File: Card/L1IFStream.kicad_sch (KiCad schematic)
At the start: 107 parts, among them J1 Conn_Coaxial, J2 USB_A, J3 RF_Shield_One_Piece, J4 Conn_Coaxial, U1 MAX2769ETI+T, U10 74LVC374, U11 74HC2GU04, U2 TPS717285DCKR, U3 TPS717285DCKR, U4 NCP164CSN330T1G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

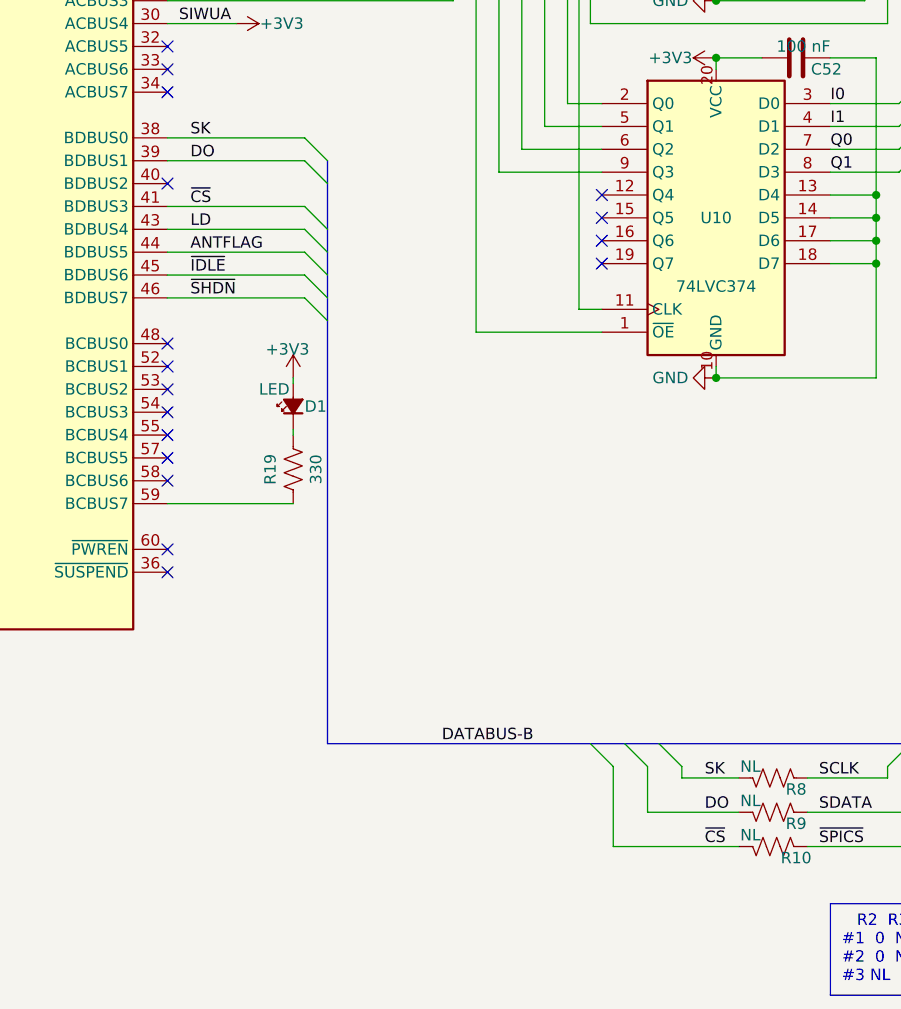
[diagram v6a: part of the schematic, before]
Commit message: Added test points to attach SPI device
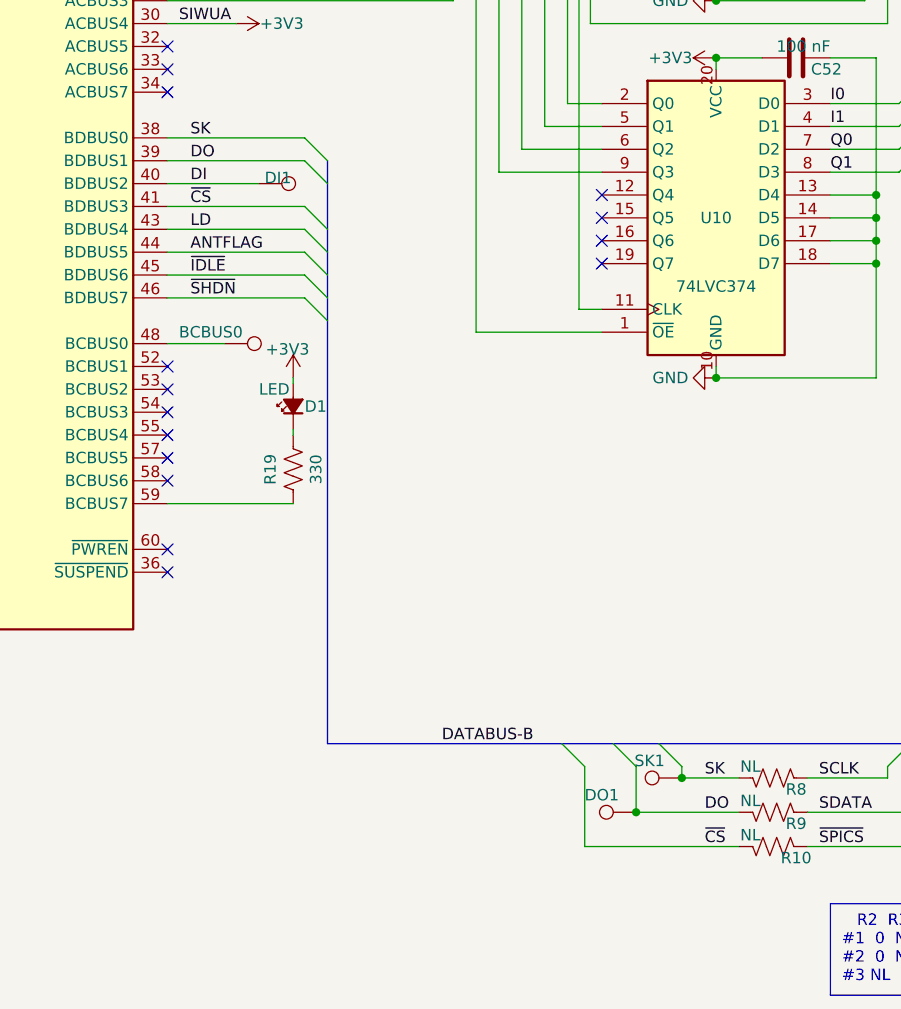
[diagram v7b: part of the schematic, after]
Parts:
- added BCBUS0, DI1, DO1, SK1: TestPoint, L1IFStream:TestPoint_Pad_D1.0mm, symbol Connector:TestPoint
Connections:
- net DO: now also DO1.1
- net SK: now also SK1.1
- net DI: now reaches U6.40 (BDBUS2)
- net DI: now also DI1.1
- net at U6.48 (BCBUS0): now also BCBUS0.1
- no-connect marks 26 -> 24
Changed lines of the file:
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@@
   (junction (at 285.75 38.1) (diameter 0) (color 0 0 0 0)
   )
+  (junction (at 196.85 182.88) (diameter 0) (color 0 0 0 0)
+  )
   (junction (at 156.21 46.99) (diameter 0) (color 0 0 0 0)
   )
@@
   (junction (at 119.38 166.37) (diameter 0) (color 0 0 0 0)
   )
+  (junction (at 201.93 179.07) (diameter 0) (color 0 0 0 0)
+  )
   (junction (at 261.62 172.72) (diameter 0) (color 0 0 0 0)
   )
@@
   )
   (no_connect (at 144.78 85.09))
-  (no_connect (at 144.78 130.81))
   (no_connect (at 193.04 119.38))
   (no_connect (at 257.81 93.98))
@@
   (no_connect (at 144.78 153.67))
   (no_connect (at 144.78 146.05))
-  (no_connect (at 144.78 113.03))
   (no_connect (at 193.04 72.39))
   (no_connect (at 144.78 100.33))
@@
     (stroke (width 0) (type default))
   )
-  (bus_entry (at 191.77 175.26) (size 2.54 2.54)
+  (bus_entry (at 188.595 175.26) (size 2.54 2.54)
     (stroke (width 0) (type default))
   )
@@
     (stroke (width 0) (type default))
   )
-  (bus_entry (at 195.58 175.26) (size 2.54 2.54)
+  (bus_entry (at 194.31 175.26) (size 2.54 2.54)
     (stroke (width 0) (type default))
   )
@@
     (stroke (width 0) (type default))
   )
-  (wire (pts (xy 198.12 182.88) (xy 198.12 177.8))
+  (wire (pts (xy 196.85 182.88) (xy 196.85 177.8))
     (stroke (width 0) (type default))
   )
@@
     (stroke (width 0) (type default))
   )
-  (bus (pts (xy 191.77 175.26) (xy 162.56 175.26))
-    (stroke (width 0) (type default))
-  )
   (wire (pts (xy 44.45 95.25) (xy 45.72 95.25))
     (stroke (width 0) (type default))
@@
     (stroke (width 0) (type default))
   )
+  (bus (pts (xy 188.595 175.26) (xy 162.56 175.26))
+    (stroke (width 0) (type default))
+  )
   (wire (pts (xy 287.02 148.59) (xy 287.02 149.86))
     (stroke (width 0) (type default))
@@
     (stroke (width 0) (type default))
   )
-  (wire (pts (xy 208.28 182.88) (xy 198.12 182.88))
-    (stroke (width 0) (type default))
-  )
   (wire (pts (xy 181.61 111.76) (xy 181.61 80.01))
     (stroke (width 0) (type default))
@@
     (stroke (width 0) (type default))
   )
+  (wire (pts (xy 144.78 113.03) (xy 154.94 113.03))
+    (stroke (width 0) (type default))
+  )
   (wire (pts (xy 111.76 166.37) (xy 114.3 166.37))
     (stroke (width 0) (type default))
@@
     (stroke (width 0) (type default))
   )
+  (wire (pts (xy 191.135 186.69) (xy 208.28 186.69))
+    (stroke (width 0) (type default))
+  )
   (bus (pts (xy 251.46 165.1) (xy 251.46 167.64))
     (stroke (width 0) (type default))
@@
     (stroke (width 0) (type default))
   )
-  (wire (pts (xy 194.31 186.69) (xy 194.31 177.8))
+  (wire (pts (xy 191.135 186.69) (xy 191.135 177.8))
     (stroke (width 0) (type default))
   )
@@
     (stroke (width 0) (type default))
   )
-  (wire (pts (xy 208.28 186.69) (xy 194.31 186.69))
-    (stroke (width 0) (type default))
-  )
   (bus (pts (xy 251.46 172.72) (xy 251.46 175.26))
     (stroke (width 0) (type default))
@@
     (stroke (width 0) (type default))
   )
+  (wire (pts (xy 196.85 182.88) (xy 208.28 182.88))
+    (stroke (width 0) (type default))
+  )
   (wire (pts (xy 123.19 34.29) (xy 123.19 33.02))
     (stroke (width 0) (type default))
@@
     (stroke (width 0) (type default))
   )
-  (bus (pts (xy 191.77 175.26) (xy 195.58 175.26))
+  (bus (pts (xy 188.595 175.26) (xy 194.31 175.26))
     (stroke (width 0) (type default))
   )
@@
     (stroke (width 0) (type default))
   )
+  (wire (pts (xy 144.78 130.81) (xy 151.13 130.81))
+    (stroke (width 0) (type default))
+  )
   (wire (pts (xy 191.77 19.05) (xy 196.85 19.05))
     (stroke (width 0) (type default))
@@
     (stroke (width 0) (type default))
   )
-  (bus (pts (xy 195.58 175.26) (xy 199.39 175.26))
+  (bus (pts (xy 194.31 175.26) (xy 199.39 175.26))
     (stroke (width 0) (type default))
   )
@@
     (effects (font (size 1.27 1.27)) (justify left bottom))
   )
+  (label "DI" (at 147.32 113.03 0) (fields_autoplaced)
+    (effects (font (size 1.27 1.27)) (justify left bottom))
+  )
   (label "LNA2" (at 245.11 78.74 180) (fields_autoplaced)
     (effects (font (size 1.27 1.27)) (justify right bottom))
@@
     )
   )
+  (symbol (lib_id "Connector:TestPoint") (at 196.85 182.88 90) (unit 1)
+    (in_bom yes) (on_board yes) (dnp no)
+    (property "Reference" "DO1" (at 194.945 180.975 90)
+      (effects (font (size 1.27 1.27)) (justify left))
+    )
+    (property "Value" "TestPoint" (at 196.1642 181.4068 0)
+      (effects (font (size 1.27 1.27)) (justify left) hide)
+    )
+    (property "Footprint" "L1IFStream:TestPoint_Pad_D1.0mm" (at 196.85 177.8 0)
+      (effects (font (size 1.27 1.27)) hide)
+    )
+    (property "Datasheet" "~" (at 196.85 177.8 0)
+      (effects (font (size 1.27 1.27)) hide)
+    )
+    (pin "1")
+    (instances
+      (project "L1IFStream"
+        (path "/e22d8814-0b83-456b-8939-db783783fcf1"
+          (reference "DO1") (unit 1)
+        )
+      )
+    )
+  )
   (symbol (lib_id "L1IFStream-rescue:74LVC374-MAX2769FT2232H") (at 205.74 116.84 0) (unit 1)
     (in_bom yes) (on_board yes) (dnp no)
@@
     )
   )
+  (symbol (lib_id "Connector:TestPoint") (at 151.13 130.81 270) (unit 1)
+    (in_bom yes) (on_board yes) (dnp no)
+    (property "Reference" "BCBUS0" (at 146.05 129.54 90)
+      (effects (font (size 1.27 1.27)) (justify left))
+    )
+    (property "Value" "TestPoint" (at 151.8158 132.2832 0)
+      (effects (font (size 1.27 1.27)) (justify left) hide)
+    )
+    (property "Footprint" "L1IFStream:TestPoint_Pad_D1.0mm" (at 151.13 135.89 0)
+      (effects (font (size 1.27 1.27)) hide)
+    )
+    (property "Datasheet" "~" (at 151.13 135.89 0)
+      (effects (font (size 1.27 1.27)) hide)
+    )
+    (pin "1")
+    (instances
+      (project "L1IFStream"
+        (path "/e22d8814-0b83-456b-8939-db783783fcf1"
+          (reference "BCBUS0") (unit 1)
+        )
+      )
+    )
+  )
   (symbol (lib_id "L1IFStream-rescue:R_US-MAX2769FT2232H") (at 331.47 87.63 0) (unit 1)
     (in_bom yes) (on_board yes) (dnp no)
@@
     )
   )
+  (symbol (lib_id "Connector:TestPoint") (at 201.93 179.07 90) (unit 1)
+    (in_bom yes) (on_board yes) (dnp no)
+    (property "Reference" "SK1" (at 200.025 177.165 90)
+      (effects (font (size 1.27 1.27)) (justify left))
+    )
+    (property "Value" "TestPoint" (at 201.2442 177.5968 0)
+      (effects (font (size 1.27 1.27)) (justify left) hide)
+    )
+    (property "Footprint" "L1IFStream:TestPoint_Pad_D1.0mm" (at 201.93 173.99 0)
+      (effects (font (size 1.27 1.27)) hide)
+    )
+    (property "Datasheet" "~" (at 201.93 173.99 0)
+      (effects (font (size 1.27 1.27)) hide)
+    )
+    (pin "1")
+    (instances
+      (project "L1IFStream"
+        (path "/e22d8814-0b83-456b-8939-db783783fcf1"
+          (reference "SK1") (unit 1)
+        )
+      )
+    )
+  )
   (symbol (lib_id "L1IFStream-rescue:C-MAX2769FT2232H") (at 335.915 83.82 90) (mirror x) (unit 1)
     (in_bom yes) (on_board yes) (dnp no)
@@
         )
       )
+    )
+  )
+  (symbol (lib_id "Connector:TestPoint") (at 154.94 113.03 270) (unit 1)
+    (in_bom yes) (on_board yes) (dnp no)
+    (property "Reference" "DI1" (at 155.575 112.395 90)
+      (effects (font (size 1.27 1.27)) (justify left))
+    )
+    (property "Value" "TestPoint" (at 155.6258 114.5032 0)
+      (effects (font (size 1.27 1.27)) (justify left) hide)
+    )
+    (property "Footprint" "L1IFStream:TestPoint_Pad_D1.0mm" (at 154.94 118.11 0)
+      (effects (font (size 1.27 1.27)) hide)
+    )
+    (property "Datasheet" "~" (at 154.94 118.11 0)
+      (effects (font (size 1.27 1.27)) hide)
+    )
+    (pin "1")
+    (instances
+      (project "L1IFStream"
+        (path "/e22d8814-0b83-456b-8939-db783783fcf1"
+          (reference "DI1") (unit 1)
+        )
+      )

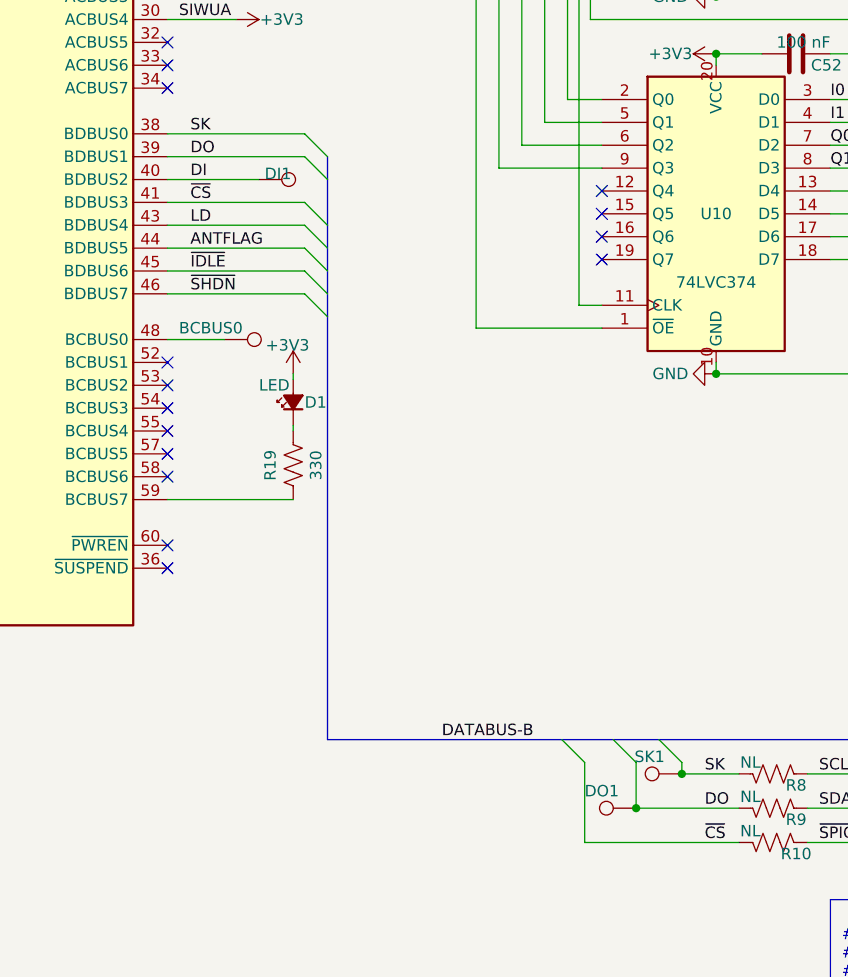
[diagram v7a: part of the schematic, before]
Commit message: Debating how much to fix. Current Argument, just the LED circuit
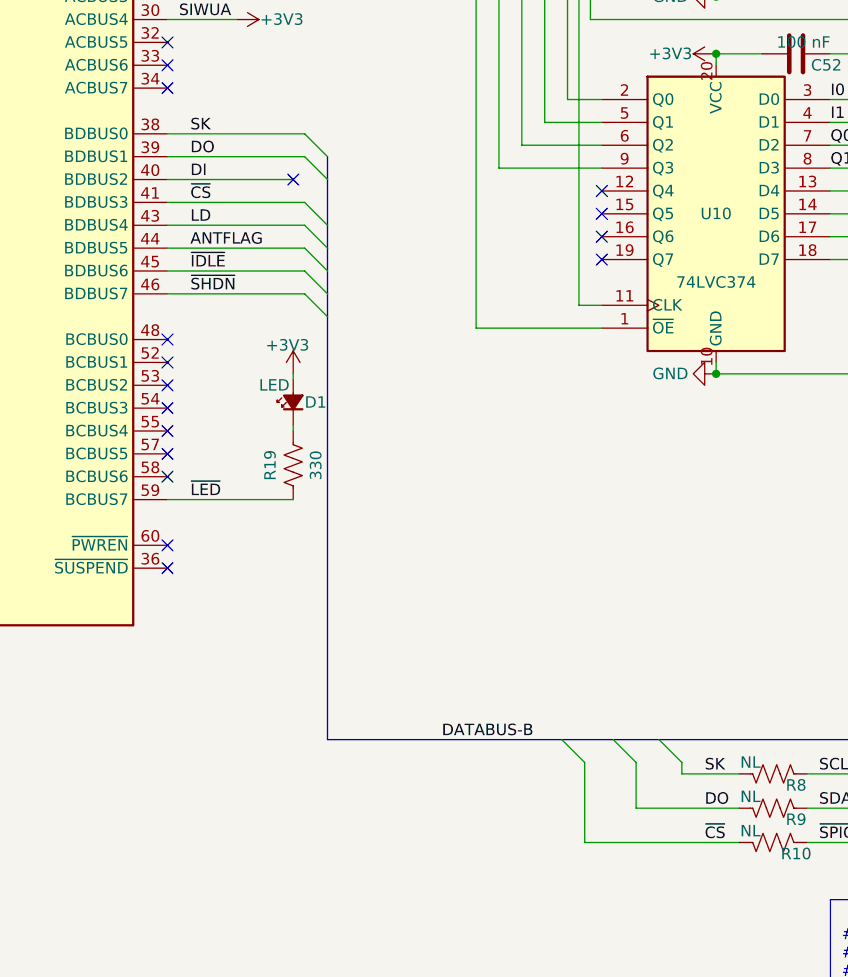
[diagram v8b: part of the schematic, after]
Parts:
- removed BCBUS0, DI1, DO1, SK1: TestPoint, L1IFStream:TestPoint_Pad_D1.0mm, symbol Connector:TestPoint
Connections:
- net ~{LED}: now reaches R19.2, U6.59 (BCBUS7)
- no-connect marks 24 -> 26
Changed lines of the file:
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@@
   (title_block
     (title "L1 IF Stream")
-    (date "2023-06-19")
+    (date "2023-10-24")
     (rev "${SCH_VER}")
     (comment 1 "creativecommons.org/licenses/by/4.0/")
@@
   (junction (at 285.75 38.1) (diameter 0) (color 0 0 0 0)
   )
-  (junction (at 196.85 182.88) (diameter 0) (color 0 0 0 0)
-  )
   (junction (at 156.21 46.99) (diameter 0) (color 0 0 0 0)
   )
@@
   (junction (at 119.38 166.37) (diameter 0) (color 0 0 0 0)
   )
-  (junction (at 201.93 179.07) (diameter 0) (color 0 0 0 0)
-  )
   (junction (at 261.62 172.72) (diameter 0) (color 0 0 0 0)
   )
@@
   (junction (at 417.83 19.05) (diameter 0) (color 0 0 0 0)
   )
+  (no_connect (at 144.78 130.81))
   (no_connect (at 144.78 85.09))
   (no_connect (at 193.04 119.38))
@@
   (no_connect (at 193.04 80.01))
   (no_connect (at 144.78 135.89))
+  (no_connect (at 158.75 113.03))
   (no_connect (at 144.78 143.51))
   (no_connect (at 144.78 138.43))
@@
     (stroke (width 0) (type default))
   )
+  (wire (pts (xy 144.78 113.03) (xy 158.75 113.03))
+    (stroke (width 0) (type default))
+  )
   (wire (pts (xy 193.04 109.22) (xy 184.15 109.22))
     (stroke (width 0) (type default))
@@
     (stroke (width 0) (type default))
   )
-  (wire (pts (xy 144.78 113.03) (xy 154.94 113.03))
-    (stroke (width 0) (type default))
-  )
   (wire (pts (xy 111.76 166.37) (xy 114.3 166.37))
     (stroke (width 0) (type default))
@@
     (stroke (width 0) (type default))
   )
-  (wire (pts (xy 144.78 130.81) (xy 151.13 130.81))
-    (stroke (width 0) (type default))
-  )
   (wire (pts (xy 191.77 19.05) (xy 196.85 19.05))
     (stroke (width 0) (type default))
@@
     (effects (font (size 1.27 1.27)) (justify left bottom))
   )
+  (label "DI" (at 147.32 113.03 0) (fields_autoplaced)
+    (effects (font (size 1.27 1.27)) (justify left bottom))
+  )
   (label "D6" (at 144.78 77.47 0) (fields_autoplaced)
     (effects (font (size 1.27 1.27)) (justify left bottom))
@@
     (effects (font (size 1.27 1.27)) (justify left bottom))
   )
-  (label "DI" (at 147.32 113.03 0) (fields_autoplaced)
-    (effects (font (size 1.27 1.27)) (justify left bottom))
-  )
   (label "LNA2" (at 245.11 78.74 180) (fields_autoplaced)
     (effects (font (size 1.27 1.27)) (justify right bottom))
@@
     (effects (font (size 1.27 1.27)) (justify left bottom))
   )
+  (label "~{LED}" (at 147.32 148.59 0) (fields_autoplaced)
+    (effects (font (size 1.27 1.27)) (justify left bottom))
+  )
   (label "2V85A" (at 322.58 97.79 0) (fields_autoplaced)
     (effects (font (size 1.27 1.27)) (justify left bottom))
@@
     )
   )
-  (symbol (lib_id "Connector:TestPoint") (at 196.85 182.88 90) (unit 1)
-    (in_bom yes) (on_board yes) (dnp no)
-    (property "Reference" "DO1" (at 194.945 180.975 90)
-      (effects (font (size 1.27 1.27)) (justify left))
-    )
-    (property "Value" "TestPoint" (at 196.1642 181.4068 0)
-      (effects (font (size 1.27 1.27)) (justify left) hide)
-    )
-    (property "Footprint" "L1IFStream:TestPoint_Pad_D1.0mm" (at 196.85 177.8 0)
-      (effects (font (size 1.27 1.27)) hide)
-    )
-    (property "Datasheet" "~" (at 196.85 177.8 0)
-      (effects (font (size 1.27 1.27)) hide)
-    )
-    (pin "1")
-    (instances
-      (project "L1IFStream"
-        (path "/e22d8814-0b83-456b-8939-db783783fcf1"
-          (reference "DO1") (unit 1)
-        )
-      )
-    )
-  )
   (symbol (lib_id "L1IFStream-rescue:74LVC374-MAX2769FT2232H") (at 205.74 116.84 0) (unit 1)
     (in_bom yes) (on_board yes) (dnp no)
@@
     )
   )
-  (symbol (lib_id "Connector:TestPoint") (at 151.13 130.81 270) (unit 1)
-    (in_bom yes) (on_board yes) (dnp no)
-    (property "Reference" "BCBUS0" (at 146.05 129.54 90)
-      (effects (font (size 1.27 1.27)) (justify left))
-    )
-    (property "Value" "TestPoint" (at 151.8158 132.2832 0)
-      (effects (font (size 1.27 1.27)) (justify left) hide)
-    )
-    (property "Footprint" "L1IFStream:TestPoint_Pad_D1.0mm" (at 151.13 135.89 0)
-      (effects (font (size 1.27 1.27)) hide)
-    )
-    (property "Datasheet" "~" (at 151.13 135.89 0)
-      (effects (font (size 1.27 1.27)) hide)
-    )
-    (pin "1")
-    (instances
-      (project "L1IFStream"
-        (path "/e22d8814-0b83-456b-8939-db783783fcf1"
-          (reference "BCBUS0") (unit 1)
-        )
-      )
-    )
-  )
   (symbol (lib_id "L1IFStream-rescue:R_US-MAX2769FT2232H") (at 331.47 87.63 0) (unit 1)
     (in_bom yes) (on_board yes) (dnp no)
@@
     )
   )
-  (symbol (lib_id "Connector:TestPoint") (at 201.93 179.07 90) (unit 1)
-    (in_bom yes) (on_board yes) (dnp no)
-    (property "Reference" "SK1" (at 200.025 177.165 90)
-      (effects (font (size 1.27 1.27)) (justify left))
-    )
-    (property "Value" "TestPoint" (at 201.2442 177.5968 0)
-      (effects (font (size 1.27 1.27)) (justify left) hide)
-    )
-    (property "Footprint" "L1IFStream:TestPoint_Pad_D1.0mm" (at 201.93 173.99 0)
-      (effects (font (size 1.27 1.27)) hide)
-    )
-    (property "Datasheet" "~" (at 201.93 173.99 0)
-      (effects (font (size 1.27 1.27)) hide)
-    )
-    (pin "1")
-    (instances
-      (project "L1IFStream"
-        (path "/e22d8814-0b83-456b-8939-db783783fcf1"
-          (reference "SK1") (unit 1)
-        )
-      )
-    )
-  )
   (symbol (lib_id "L1IFStream-rescue:C-MAX2769FT2232H") (at 335.915 83.82 90) (mirror x) (unit 1)
     (in_bom yes) (on_board yes) (dnp no)
@@
         )
       )
-    )
-  )
-  (symbol (lib_id "Connector:TestPoint") (at 154.94 113.03 270) (unit 1)
-    (in_bom yes) (on_board yes) (dnp no)
-    (property "Reference" "DI1" (at 155.575 112.395 90)
-      (effects (font (size 1.27 1.27)) (justify left))
-    )
-    (property "Value" "TestPoint" (at 155.6258 114.5032 0)
-      (effects (font (size 1.27 1.27)) (justify left) hide)
-    )
-    (property "Footprint" "L1IFStream:TestPoint_Pad_D1.0mm" (at 154.94 118.11 0)
-      (effects (font (size 1.27 1.27)) hide)
-    )
-    (property "Datasheet" "~" (at 154.94 118.11 0)
-      (effects (font (size 1.27 1.27)) hide)
-    )
-    (pin "1")
-    (instances
-      (project "L1IFStream"
-        (path "/e22d8814-0b83-456b-8939-db783783fcf1"
-          (reference "DI1") (unit 1)
-        )
-      )
